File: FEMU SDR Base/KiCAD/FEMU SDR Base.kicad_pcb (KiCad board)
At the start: 2 copper layers, 164.8 x 164.8 mm, 0 parts

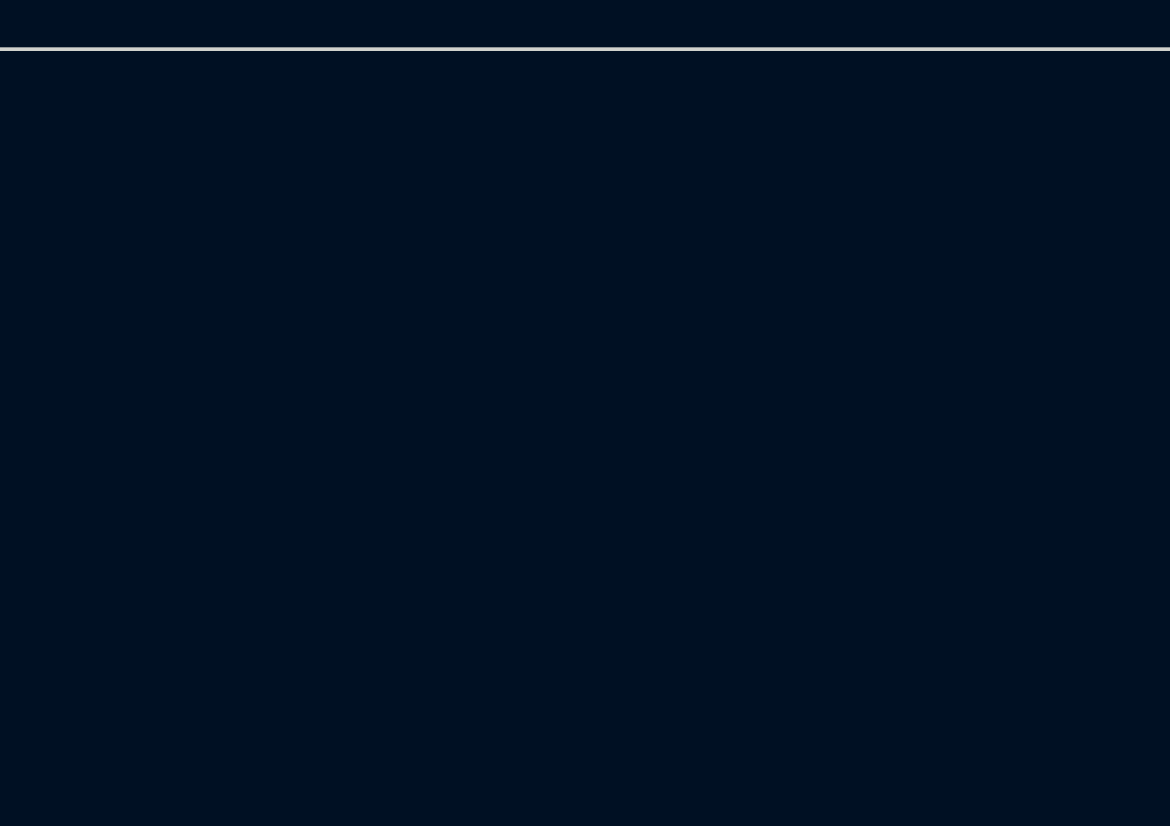
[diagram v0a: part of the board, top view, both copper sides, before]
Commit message: STATUS = FREE ; pcbnew layout of RasPi PSU added, Changed to 4 layers.
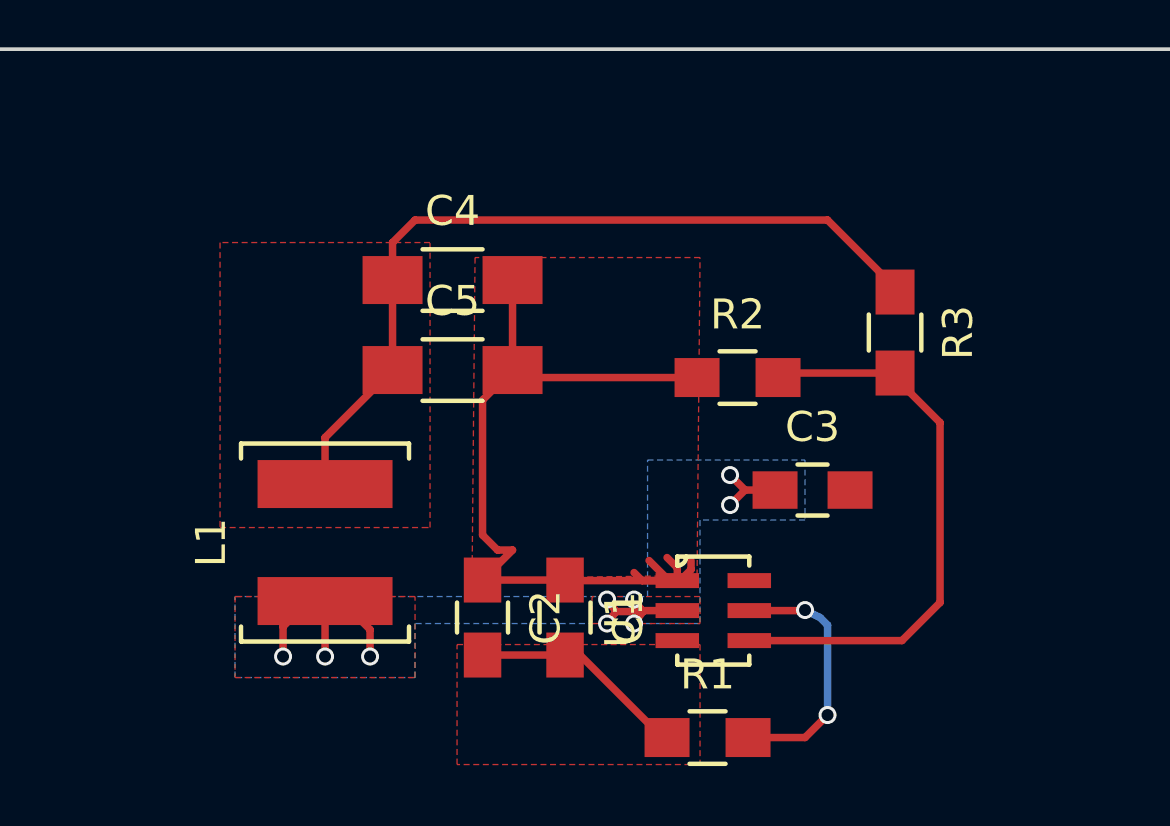
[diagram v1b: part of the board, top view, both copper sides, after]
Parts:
- added C1: 10u, Capacitors_SMD:C_0805_HandSoldering, F.Cu at (94.5, 176.0)
- added C2: 10u, Capacitors_SMD:C_0805_HandSoldering, F.Cu at (91.8, 176.0)
- added C3: 0.1u, Capacitors_SMD:C_0805_HandSoldering, F.Cu at (102.8, 171.8)
- added C4: 33u, Capacitors_SMD:C_1206_HandSoldering, F.Cu at (90.8, 164.8)
- added C5: 33u, Capacitors_SMD:C_1206_HandSoldering, F.Cu at (90.8, 167.8)
- added L1: 4.7u, ARB_foots:L_Wurth_74404052039, F.Cu at (86.5, 173.5)
- added R1: 10k, Resistors_SMD:R_0805_HandSoldering, F.Cu at (99.2, 180.0)
- added R2: 10k, Resistors_SMD:R_0805_HandSoldering, F.Cu at (100.2, 168.0)
- added R3: 56k, Resistors_SMD:R_0805_HandSoldering, F.Cu at (105.5, 166.5)
- added U1: TPS562209, ARB_foots:TPS562209, F.Cu at (99.4, 175.8)
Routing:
- net Earth: track 0.00 -> 28.9 mm
- net +5V: track 0.00 -> 27.1 mm
- net Net-(R2-Pad2): track 0.00 -> 19.1 mm
- net /VSW: track 0.00 -> 14.4 mm, vias 0 -> 9
- net Net-(R1-Pad2): track 0.00 -> 8.73 mm, vias 0 -> 2
- net +12V: track 0.00 -> 7.29 mm
- added copper zone on F.Cu, net +12V
- added copper zone on F.Cu, net +5V
- added copper zone on B.Cu, net /VSW
- added copper zone on F.Cu, net /VSW
- added copper zone on F.Cu, net Earth
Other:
- copper layers 2 -> 4

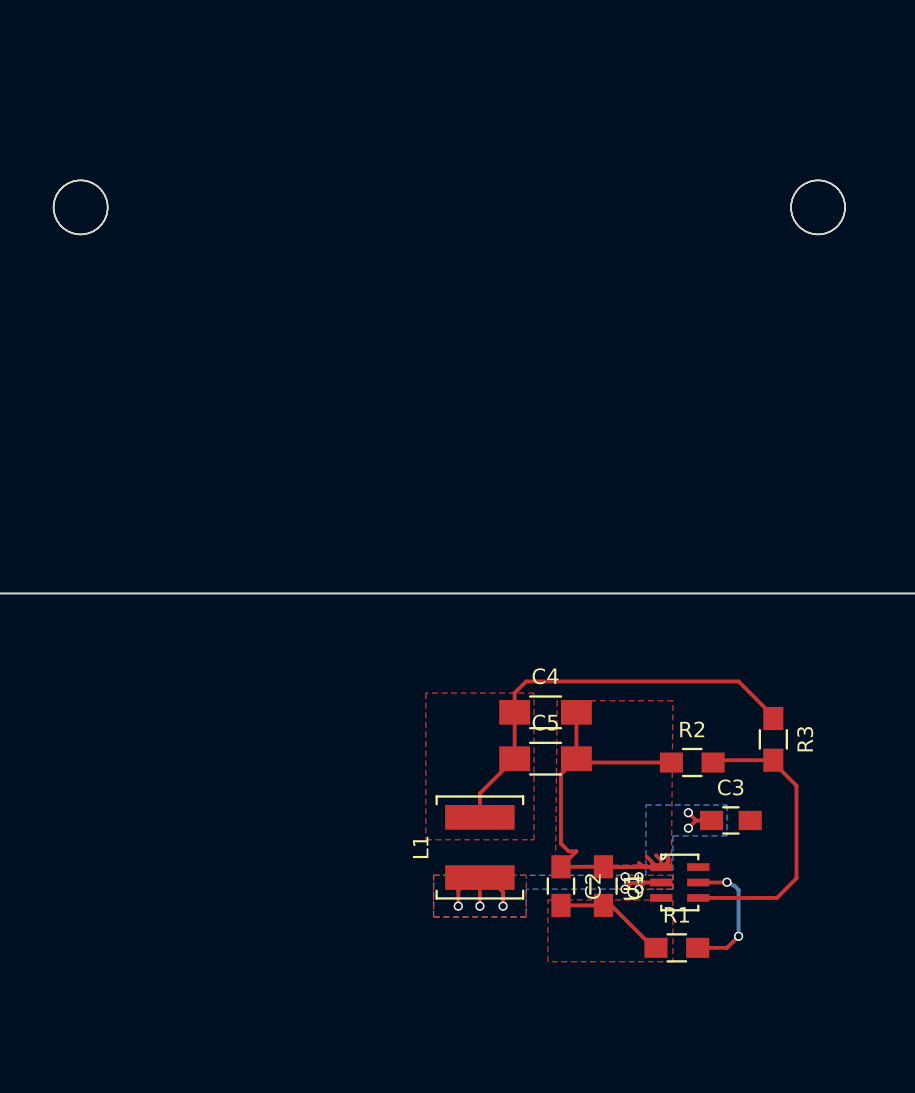
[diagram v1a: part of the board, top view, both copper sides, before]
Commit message: added footprints and some elements to netlist
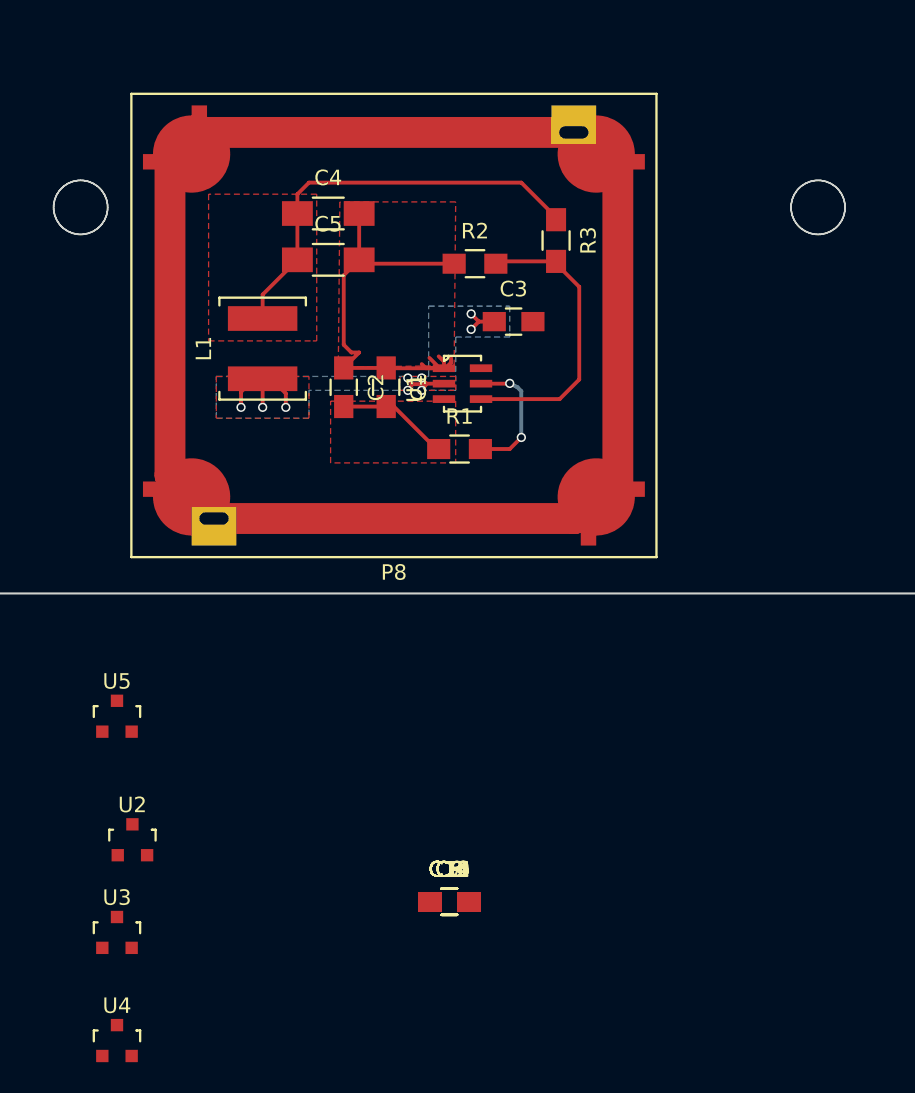
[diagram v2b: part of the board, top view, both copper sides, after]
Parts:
- added C10, C11, C12, C13, C14, C15, C16, C9: 1uF, Capacitors_SMD:C_0805_HandSoldering, F.Cu at (84.5, 177.0)
- added C6: 100nF, Capacitors_SMD:C_0805_HandSoldering, F.Cu at (84.5, 177.0)
- added C7: 1nF, Capacitors_SMD:C_0805_HandSoldering, F.Cu at (84.5, 177.0)
- added C8: 100pF, Capacitors_SMD:C_0805_HandSoldering, F.Cu at (84.5, 177.0)
- added P8: Raspi_Power_Shield, ARB_foots:PCB_Shield_29x25mm, F.Cu at (80.9, 139.7)
- added U2: SDR_1_LDO_1_2V, TO_SOT_Packages_SMD:SOT-23, F.Cu at (64.0, 173.0)
- added U3: SDR_2_LDO_1_2V, TO_SOT_Packages_SMD:SOT-23, F.Cu at (63.0, 179.0)
- added U4: SDR_1_LDO_3_3V, TO_SOT_Packages_SMD:SOT-23, F.Cu at (63.0, 186.0)
- added U5: SDR_2_LDO_3_3V, TO_SOT_Packages_SMD:SOT-23, F.Cu at (63.0, 165.0)
- R1: value 10k -> 100
- R3: value 56k -> 54.9k
- moved C1 35.2 mm to (80.4, 143.7)
- moved C2 35.2 mm to (77.7, 143.7)
- moved C3 35.2 mm to (88.7, 139.4)
- moved C4 35.2 mm to (76.7, 132.4)
- moved C5 35.2 mm to (76.7, 135.4)
- moved L1 35.2 mm to (72.4, 141.2)
- moved R1 35.2 mm to (85.2, 147.7)
- moved R2 35.2 mm to (86.2, 135.7)
- moved R3 35.2 mm to (91.4, 134.2)
- moved U1 35.2 mm to (85.4, 143.5)
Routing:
- net GND: track 0.00 -> 99.8 mm

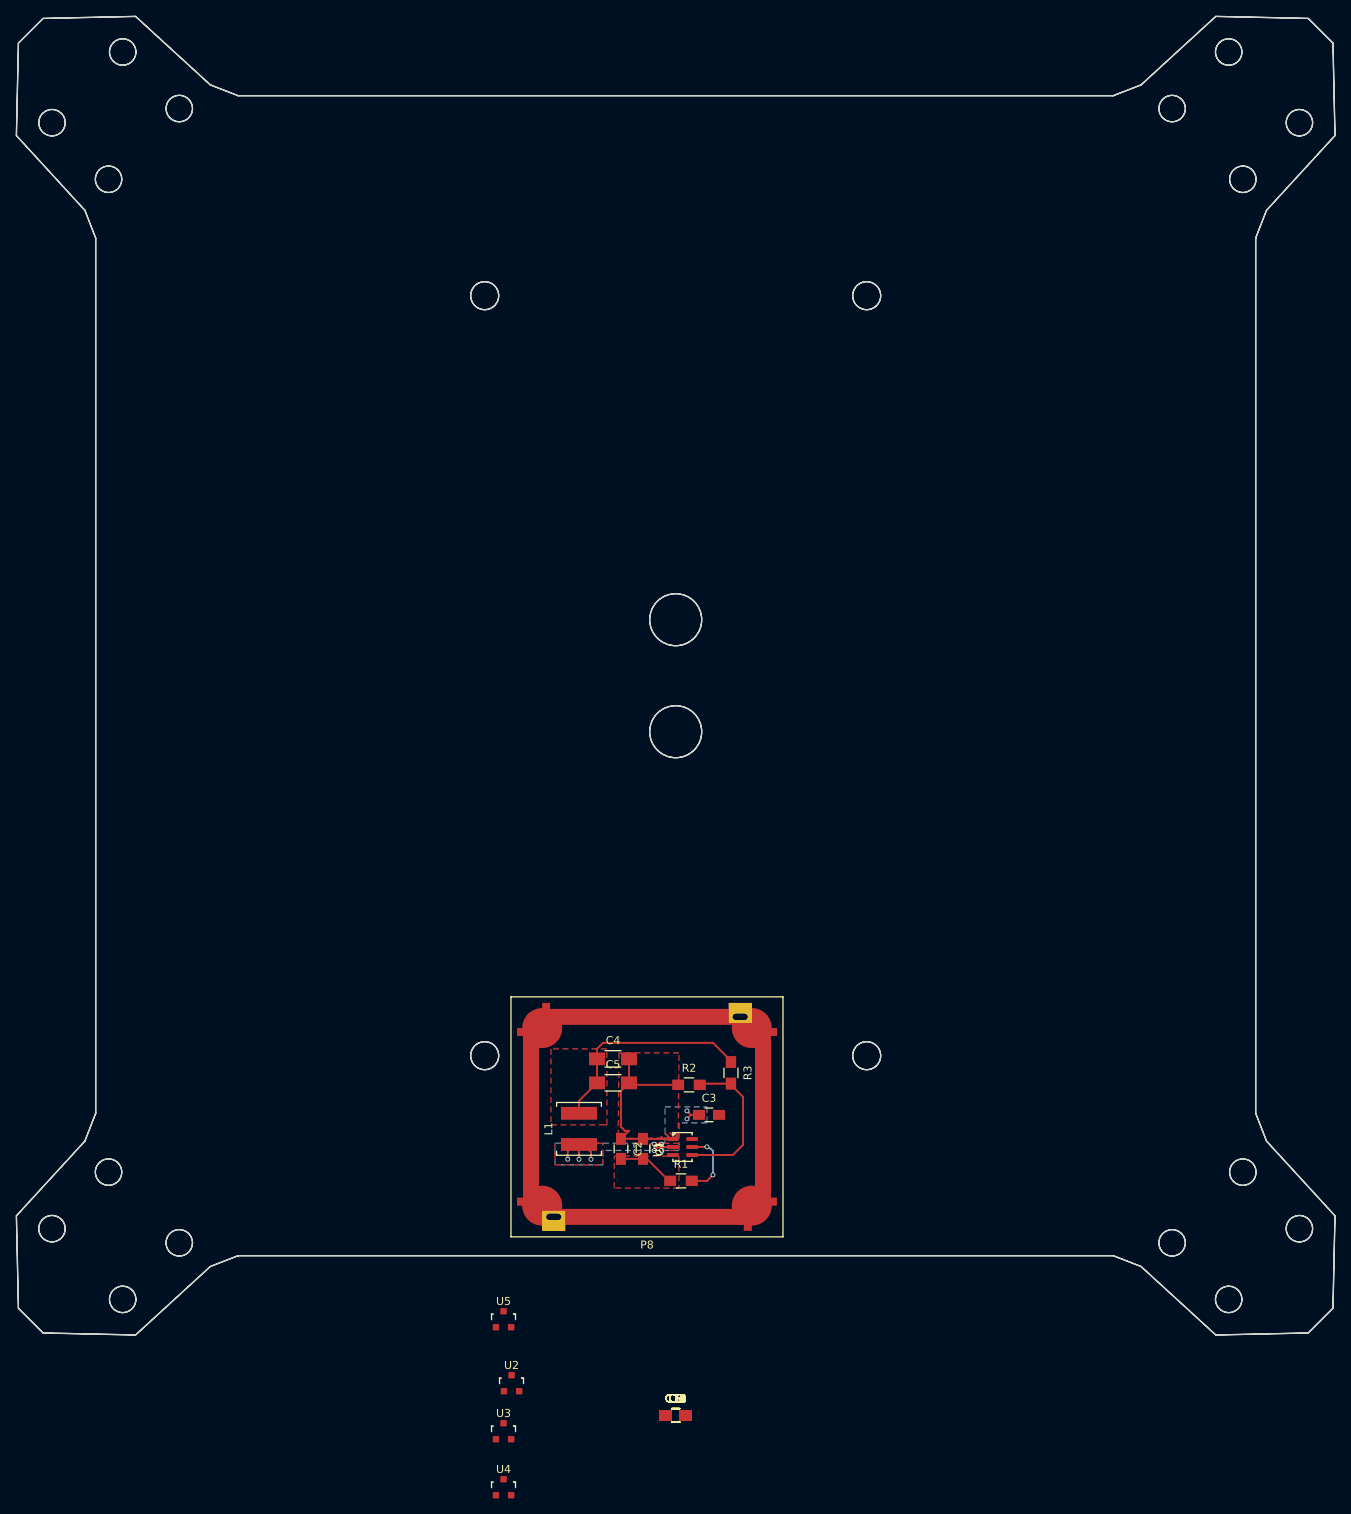
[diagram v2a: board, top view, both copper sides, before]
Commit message: added SDR LDO components and edited RasPi PSU shield footprint
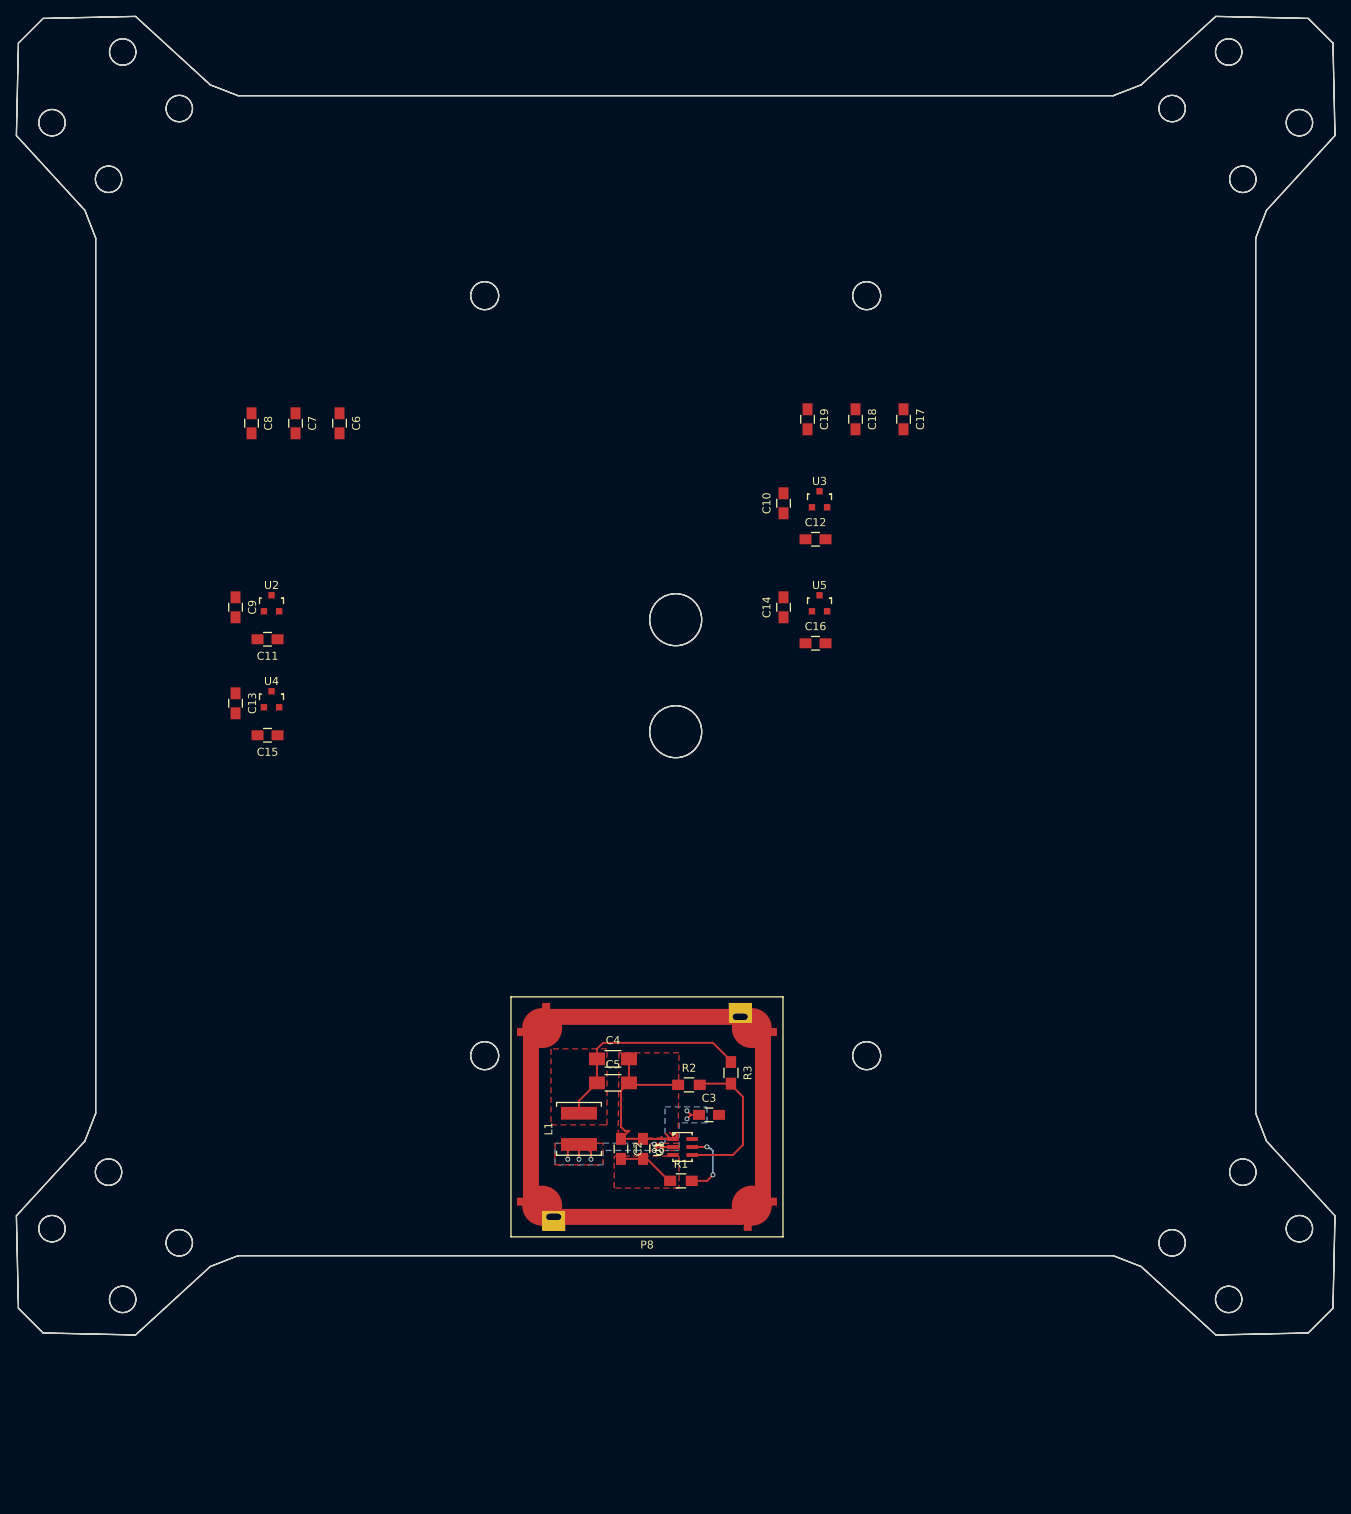
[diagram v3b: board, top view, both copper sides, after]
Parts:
- added C17: 100nF, Capacitors_SMD:C_0805_HandSoldering, F.Cu at (113.0, 52.5)
- added C18: 1nF, Capacitors_SMD:C_0805_HandSoldering, F.Cu at (107.0, 52.5)
- added C19: 100pF, Capacitors_SMD:C_0805_HandSoldering, F.Cu at (101.0, 52.5)
- moved C8 134.9 mm to (31.5, 53.0), turned to 270 degrees
- moved C7 132.8 mm to (37.0, 53.0), turned to 270 degrees
- moved C6 130.9 mm to (42.5, 53.0), turned to 270 degrees
- moved U3 123.0 mm to (102.5, 62.5)
- moved C9 115.0 mm to (29.5, 76.0), turned to 270 degrees
- moved C10 114.8 mm to (98.0, 63.0), turned to 90 degrees
- moved C12 110.9 mm to (102.0, 67.5)
- moved C11 109.6 mm to (33.5, 80.0), turned to 180 degrees
- moved C13 104.6 mm to (29.5, 88.0), turned to 270 degrees
- moved U4 102.7 mm to (34.0, 87.5)
- moved U2 102.0 mm to (34.0, 75.5)
- moved C14 101.9 mm to (98.0, 76.0), turned to 90 degrees
- moved C15 99.2 mm to (33.5, 92.0), turned to 180 degrees
- moved C16 98.1 mm to (102.0, 80.5)
- moved U5 97.8 mm to (102.5, 75.5)
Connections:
- C11 pad 1: +1V2 -> +1V2_SDR1
- C12 pad 2: +1V2 -> +1V2_SDR2
- C15 pad 1: +3V3 -> +3V3_SDR1
- C16 pad 2: +3V3 -> +3V3_SDR2
- U2 pad 2: +1V2 -> +1V2_SDR1
- U3 pad 2: +1V2 -> +1V2_SDR2
- U4 pad 2: +3V3 -> +3V3_SDR1
- U5 pad 2: +3V3 -> +3V3_SDR2
